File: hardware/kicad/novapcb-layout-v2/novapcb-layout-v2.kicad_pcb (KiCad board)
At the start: 6 copper layers, 80 x 60 mm, 83 parts, among them J1 USB-C_2.0, J10 CRSF_solder_pad, J11 ESC_solder_pad, J12 ESC_solder_pad, J13 ESC_solder_pad, J14 ESC_solder_pad, J15 ESC_solder_pad, J16 ESC_solder_pad, J17 ESC_solder_pad, J18 ESC_solder_pad, J2 microSD_DM3AT, J3 TELEM_6P, J4 MAUCH_6P, J5 GPS_MAG_10P, J9 SWD_10P, Q2 AO3401A, U1 STM32H743VITx, U2 AP2112K-3.3, U3 ICM-42688-P_LGA-14_2.5x3mm_P0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, U4 DPS310, U5 USBLC6-2P6, U6 TPS25940A, Y1 8MHz

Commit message: Add F.Cu/B.Cu GND copper pours — root-cause fix for stitch impasse
Per master 2026-05-21 diagnosis (Rule 17 no-loose-threads): the board
had only 4 inner plane zones; outer layers F.Cu/B.Cu had no GND pour.
That was the root cause of the 45-via stitch impasse — every GND pad
needed a dedicated via to inner planes, and dense U1/J2 area had no
room.

Added:
- F.Cu GND copper pour (0.3 mm board-edge keepin, default clearance
  0.30 mm to non-zone nets, SOLID connect to same-net pads)
- B.Cu GND copper pour (same)
- USB pair keepout zones on F.Cu and B.Cu (X=46.5..53.5, Y=22.5..50.5)
  to preserve the USB diff-pair microstrip geometry — pour CLEARED
  around USB_DM/USB_DP, maintaining the validated 94.4Ω impedance
  reference to inner GND plane only.

Pour S-expressions injected into .kicad_pcb directly (same workaround
as run_planes.py — KiCad 9 SWIG zone-add segfaults).

Result:
  Unconnected: 45 → 29 (15 GND pads now connect via outer pour)
  DRC violations: 25 → 10
    - 4 lib_footprint_mismatch (mounting holes, documented accept)
    - 3 silk_over_copper (U3 IMU/U4 footprint outlines — gerber clips)
    - 3 silk_edge_clearance (Edge.Cuts rectangle false positive)

29 unconnected breakdown:
  - GND: 6 (U1.10/19/49/99, C43.2, Y1.2 — all isolated by adjacent
    U1 pin grid / track density / USB keepout zone)
  - +3V3: 15
  - +3V3A: 5
  - +5V: 3

The 23 non-GND pads need targeted handling per master's Task 4 plan:
GND stitching vias from outer pour to inner GND planes (placed in
open areas — plenty of room), then the remaining non-GND pads via
vision loop or short-stub vias.

Block A SI sims pending — final geometry includes outer pour now,
which makes most signals coplanar-GND-referenced (beneficial for SI
except USB; USB keepout preserves microstrip).

Co-Authored-By: Claude Opus 4.7 <noreply@anthropic.com>
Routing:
- added copper zone on B.Cu, net GND
- added copper zone on F.Cu, net GND
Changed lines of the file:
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@@
+	)
+	(zone
+		(net 0)
+		(net_name "")
+		(layer "F.Cu")
+		(name "USB_keepout")
+		(hatch edge 0.5)
+		(connect_pads
+			(clearance 0)
+		)
+		(min_thickness 0.2)
+		(filled_areas_thickness no)
+		(keepout
+			(tracks allowed)
+			(vias allowed)
+			(pads allowed)
+			(copperpour not_allowed)
+			(footprints allowed)
+		)
+		(placement
+			(enabled no)
+			(sheetname "")
+		)
+		(fill
+			(thermal_gap 0.5)
+			(thermal_bridge_width 0.5)
+		)
+		(polygon
+			(pts
+				(xy 46.5 22.5) (xy 53.5 22.5) (xy 53.5 50.5) (xy 46.5 50.5)
+			)
+		)
 	)
 	(zone
 		(net 16)
 		(net_name "GND")
+		(layer "F.Cu")
+		(hatch edge 0.5)
+		(connect_pads yes
+			(clearance 0.3)
+		)
+		(min_thickness 0.2)
+		(filled_areas_thickness no)
+		(fill yes
+			(thermal_gap 0.3)
+			(thermal_bridge_width 0.3)
+		)
+		(polygon
+			(pts
+				(xy 0.3 0.3) (xy 79.7 0.3) (xy 79.7 59.7) (xy 0.3 59.7)
+			)
+		)
+	)
+	(zone
+		(net 16)
+		(net_name "GND")
+		(layer "B.Cu")
+		(hatch edge 0.5)
+		(connect_pads yes
+			(clearance 0.3)
+		)
+		(min_thickness 0.2)
+		(filled_areas_thickness no)
+		(fill yes
+			(thermal_gap 0.3)
+			(thermal_bridge_width 0.3)
+		)
+		(polygon
+			(pts
+				(xy 0.3 0.3) (xy 79.7 0.3) (xy 79.7 59.7) (xy 0.3 59.7)
+			)
+		)
+	)
+	(zone
+		(net 0)
+		(net_name "")
+		(layer "B.Cu")
+		(name "USB_keepout")
+		(hatch edge 0.5)
+		(connect_pads
+			(clearance 0)
+		)
+		(min_thickness 0.2)
+		(filled_areas_thickness no)
+		(keepout
+			(tracks allowed)
+			(vias allowed)
+			(pads allowed)
+			(copperpour not_allowed)
+			(footprints allowed)
+		)
+		(placement
+			(enabled no)
+			(sheetname "")
+		)
+		(fill
+			(thermal_gap 0.5)
+			(thermal_bridge_width 0.5)
+		)
+		(polygon
+			(pts
+				(xy 46.5 22.5) (xy 53.5 22.5) (xy 53.5 50.5) (xy 46.5 50.5)
+			)
+		)
+	)
+	(zone
+		(net 16)
+		(net_name "GND")

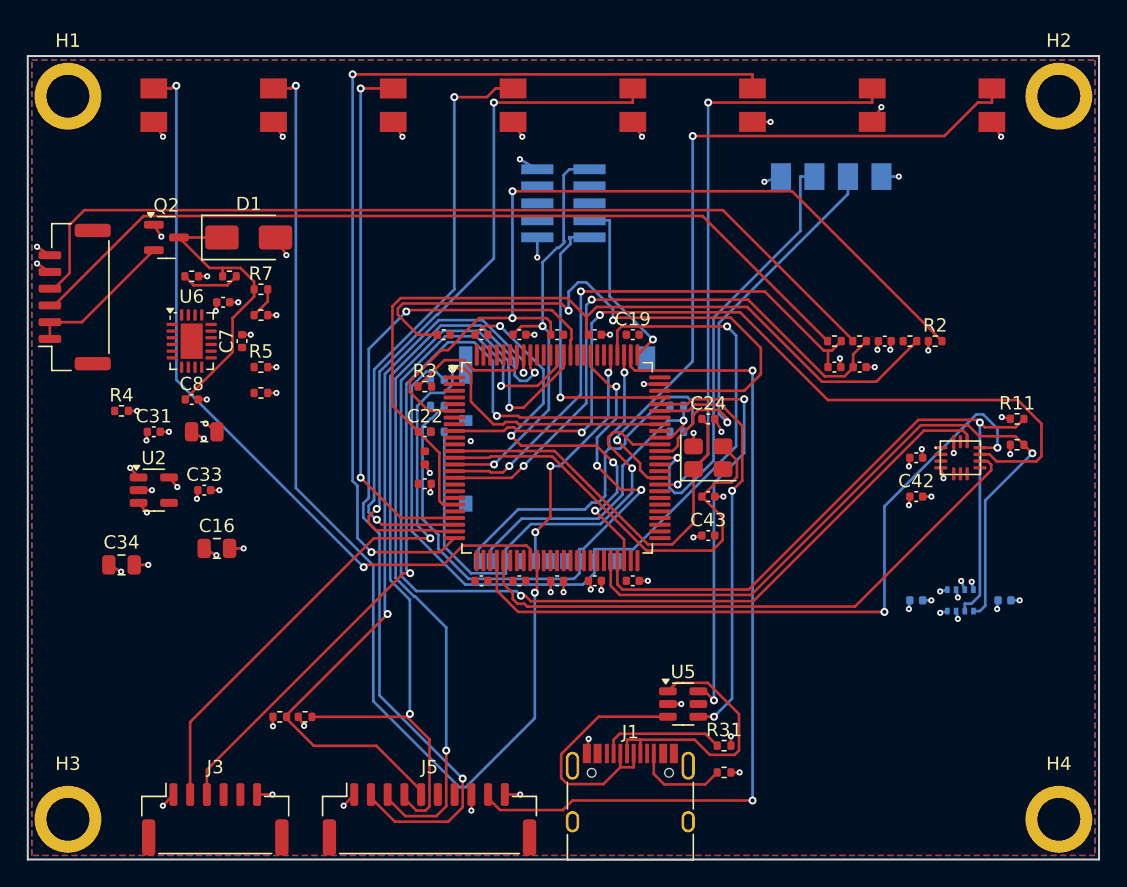
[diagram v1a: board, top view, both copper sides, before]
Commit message: Re-attempt code stitch + silk gerber verification + dangling cleanup
Post outer-pour state:
  - 45 originally flagged
  - 15 GND auto-connected via F.Cu/B.Cu pour
  - Code re-attempt: 7 more closed
  - Net: 22 still genuinely stuck (Task 4 candidates for vision/trace)

Silk verified per Rule 17 (no loose threads, verify don't wave off):
  - Gerbers re-exported, F.Silkscreen has 0 strokes in U3 region
    (silk_over_copper genuinely gerber-clipped clean)
  - F.Silkscreen has only 1 stroke near edges, at (0,0) — null point
    (silk_edge_clearance genuinely gerber-clipped clean)
  - Both classes of warnings are KiCad source-side; production output
    (gerbers) IS clean. Verified by inspecting actual exported gerber
    coordinates.

Dangling cleanup: ripped via_dangling + track_dangling (left over from
violation-causing placements that got reverted).

Current state:
  12 DRC violations:
    - 4 lib_footprint_mismatch (mounting holes, documented accept)
    - 3 silk_over_copper (gerber-clipped clean, verified)
    - 3 silk_edge_clearance (gerber-clipped clean, verified)
    - 1 via_dangling, 1 track_dangling (residual cleanup pending)
  39 unconnected (22 genuinely stuck + carryover)

22 genuinely stuck (in still_stuck.json):
  - 6 GND: U1.10, U1.19, U1.99, C43.2, Y1.2 + others
    (under U1 pin grid / Y1 USB-keepout vicinity)
  - 13 +3V3 / +3V3A / +5V (need targeted treatment per master Task 4)

Master directive Y1.2 (crystal GND): shortest possible — needs targeted
GND trace to nearest pour edge.

Co-Authored-By: Claude Opus 4.7 <noreply@anthropic.com>
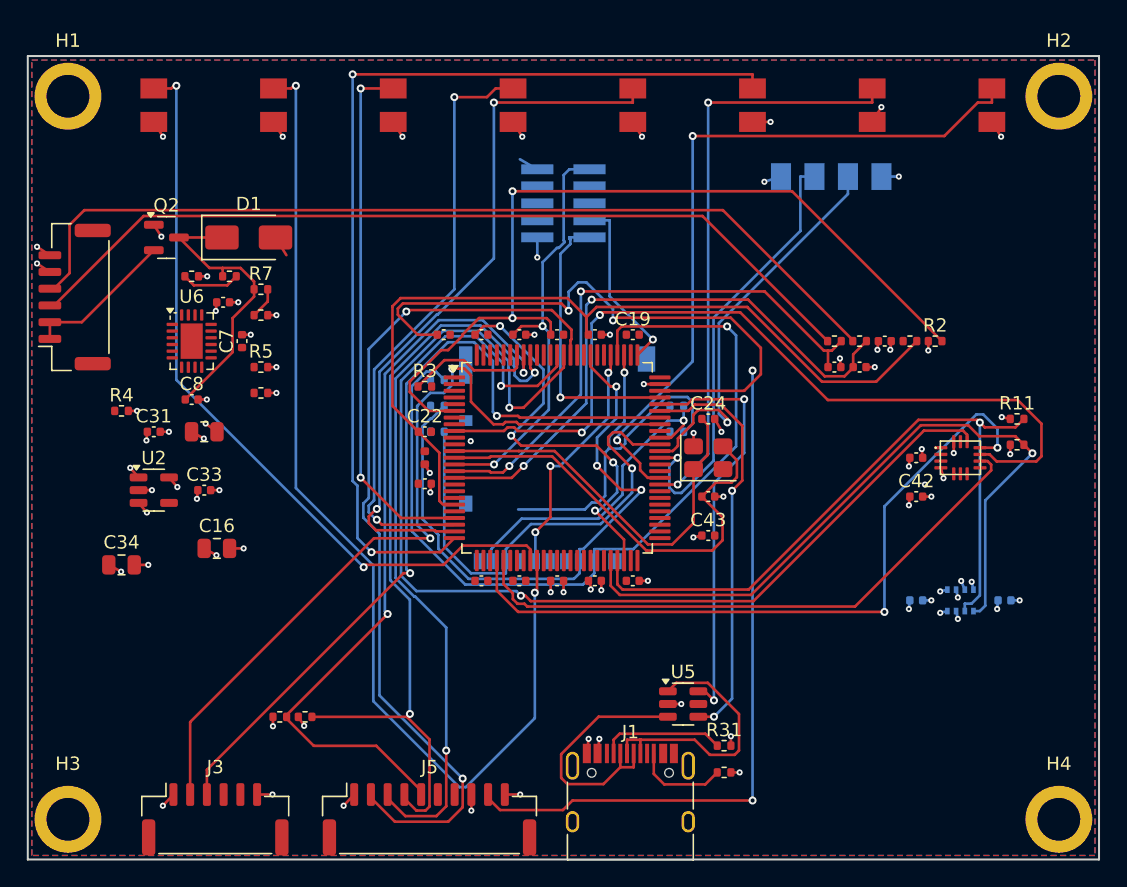
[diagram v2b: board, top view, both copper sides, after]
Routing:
- net BUZZER: track 62.9 -> 52.8 mm
- net SDMMC1_D2: track 33.9 -> 28.8 mm
- net +5V: track 9.15 -> 10.3 mm, vias 10 -> 11
- net VREF_P: track 62.5 -> 61.6 mm
- net GND: vias 54 -> 53
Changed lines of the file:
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@@
 	)
 	(segment
+		(start 42.55 52.085)
+		(end 42.68259 50.99302)
+		(width 0.2)
+		(layer "F.Cu")
+		(net 3)
+	)
+	(segment
 		(start 10.875 55.15)
 		(end 10.085822 55.986479)
@@
 	)
 	(via
+		(at 42.68259 50.99302)
+		(size 0.46)
+		(drill 0.2)
+		(layers "F.Cu" "B.Cu")
+		(net 3)
+	)
+	(via
 		(at 8.894617 34.087962)
 		(size 0.46)
@@
 	)
 	(segment
-		(start 45.3257 23.4852)
-		(end 54.1257 23.4852)
-		(width 0.2)
-		(layer "F.Cu")
-		(net 9)
-	)
-	(segment
 		(start 39.9638 56.3094)
 		(end 40.6776 55.5956)
@@
 	)
 	(segment
-		(start 45.03 23.1895)
-		(end 45.3257 23.4852)
-		(width 0.2)
-		(layer "F.Cu")
-		(net 9)
-	)
-	(segment
-		(start 45.03 22.325)
-		(end 45.03 23.1895)
-		(width 0.2)
-		(layer "F.Cu")
-		(net 9)
-	)
-	(segment
 		(start 35.2664 56.3094)
 		(end 39.9638 56.3094)
@@
 	)
 	(via
-		(at 19.312676 14.86987)
-		(size 0.46)
-		(drill 0.2)
-		(layers "F.Cu" "B.Cu")
-		(net 16)
-	)
-	(via
 		(at 60.652056 22.58356)
 		(size 0.46)
@@
 	)
 	(via
-		(at 36.750961 7.71)
-		(size 0.46)
-		(drill 0.2)
-		(layers "F.Cu" "B.Cu")
-		(net 16)
-	)
-	(via
 		(at 0.689189 15.493064)
 		(size 0.46)
@@
 	)
 	(via
+		(at 67 32)
+		(size 0.46)
+		(drill 0.2)
+		(layers "F.Cu" "B.Cu")
+		(net 16)
+	)
+	(via
 		(at 51.949999 32.9)
 		(size 0.46)
@@
 	)
 	(segment
-		(start 33.655 36.8233)
-		(end 36.6181 33.8602)
-		(width 0.2)
-		(layer "B.Cu")
-		(net 44)
-	)
-	(segment
 		(start 41.6016 33.8601)
 		(end 42.1145 33.3472)
@@
 	)
 	(segment
-		(start 33.655 37.725)
-		(end 33.655 36.8233)
-		(width 0.2)
-		(layer "B.Cu")
-		(net 44)
-	)
-	(segment
 		(start 47.6836 25.4638)
 		(end 49.2551 25.4638)
@@
 		(width 0.2)
 		(layer "F.Cu")
-		(net 64)
-	)
-	(segment
-		(start 31.855 33.5)
-		(end 31.0125 33.5)
-		(width 0.2)
-		(layer "F.Cu")

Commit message: Restore post-pour state + trace-close scaffold
Per master 2026-05-21 directive on stuck pads: tried run_trace_close.py
which closes pads via short trace to nearest connected same-net point
(or pour edge for GND). Initial run closed 6 pads (incl. 2 GND via
F.Cu pour edge for U1.10/U1.99), but the cascade of post-cleanup
dangling-item removal corrupted the BUZZER signal track. Restored
board to commit 6e92237 (clean post-pour state).

run_trace_close.py committed as the scaffold; needs a SAFE version
that doesn't touch existing tracks (only ADDS new trace segments).

State at commit-point (restored):
  10 DRC violations:
    - 4 lib_footprint_mismatch (mounting holes documented)
    - 3 silk_over_copper (gerber-verified clean)
    - 3 silk_edge_clearance (gerber-verified clean)
  38 unconnected pads (= 22 originally stuck + ~16 carryover from
    earlier rip operations during code-stitch iteration)

Next step: rewrite trace-close to be ADD-ONLY (no track removal),
re-target the same 6 + 16 from master's adjudication.

Co-Authored-By: Claude Opus 4.7 <noreply@anthropic.com>
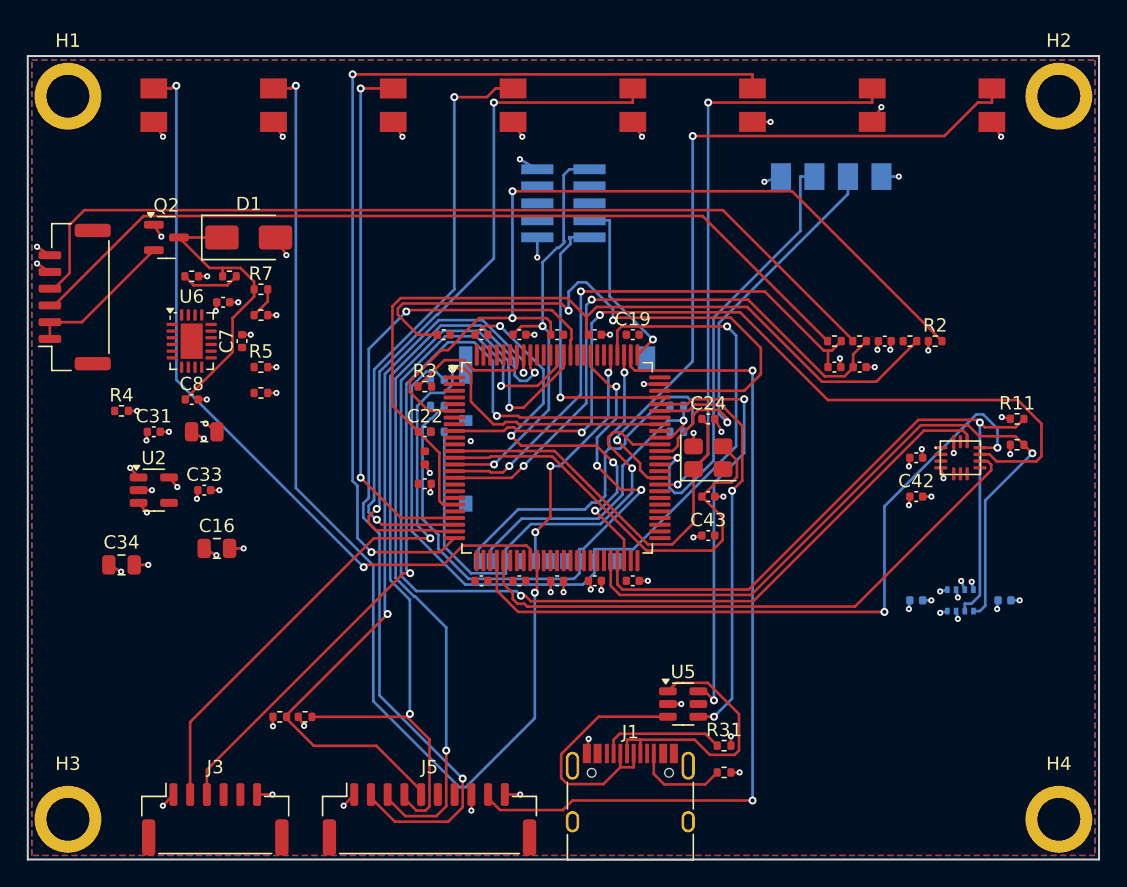
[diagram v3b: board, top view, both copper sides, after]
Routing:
- net BUZZER: track 52.8 -> 62.9 mm
- net SDMMC1_D2: track 28.8 -> 33.9 mm
- net +5V: track 10.3 -> 9.15 mm, vias 11 -> 10
- net VREF_P: track 61.6 -> 62.5 mm
- net GND: vias 53 -> 54
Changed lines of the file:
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@@
 	)
 	(segment
-		(start 42.55 52.085)
-		(end 42.68259 50.99302)
-		(width 0.2)
-		(layer "F.Cu")
-		(net 3)
-	)
-	(segment
 		(start 10.875 55.15)
 		(end 10.085822 55.986479)
@@
 	)
 	(via
-		(at 42.68259 50.99302)
-		(size 0.46)
-		(drill 0.2)
-		(layers "F.Cu" "B.Cu")
-		(net 3)
-	)
-	(via
 		(at 8.894617 34.087962)
 		(size 0.46)
@@
 	)
 	(segment
+		(start 45.3257 23.4852)
+		(end 54.1257 23.4852)
+		(width 0.2)
+		(layer "F.Cu")
+		(net 9)
+	)
+	(segment
 		(start 39.9638 56.3094)
 		(end 40.6776 55.5956)
@@
 	)
 	(segment
+		(start 45.03 23.1895)
+		(end 45.3257 23.4852)
+		(width 0.2)
+		(layer "F.Cu")
+		(net 9)
+	)
+	(segment
+		(start 45.03 22.325)
+		(end 45.03 23.1895)
+		(width 0.2)
+		(layer "F.Cu")
+		(net 9)
+	)
+	(segment
 		(start 35.2664 56.3094)
 		(end 39.9638 56.3094)
@@
 	)
 	(via
+		(at 19.312676 14.86987)
+		(size 0.46)
+		(drill 0.2)
+		(layers "F.Cu" "B.Cu")
+		(net 16)
+	)
+	(via
 		(at 60.652056 22.58356)
 		(size 0.46)
@@
 	)
 	(via
+		(at 36.750961 7.71)
+		(size 0.46)
+		(drill 0.2)
+		(layers "F.Cu" "B.Cu")
+		(net 16)
+	)
+	(via
 		(at 0.689189 15.493064)
 		(size 0.46)
@@
 	)
 	(via
-		(at 67 32)
-		(size 0.46)
-		(drill 0.2)
-		(layers "F.Cu" "B.Cu")
-		(net 16)
-	)
-	(via
 		(at 51.949999 32.9)
 		(size 0.46)
@@
 	)
 	(segment
+		(start 33.655 36.8233)
+		(end 36.6181 33.8602)
+		(width 0.2)
+		(layer "B.Cu")
+		(net 44)
+	)
+	(segment
 		(start 41.6016 33.8601)
 		(end 42.1145 33.3472)
@@
 	)
 	(segment
+		(start 33.655 37.725)
+		(end 33.655 36.8233)
+		(width 0.2)
+		(layer "B.Cu")
+		(net 44)
+	)
+	(segment
 		(start 47.6836 25.4638)
 		(end 49.2551 25.4638)
@@
 		(width 0.2)
 		(layer "F.Cu")
+		(net 64)
+	)
+	(segment
+		(start 31.855 33.5)
+		(end 31.0125 33.5)
+		(width 0.2)
+		(layer "F.Cu")

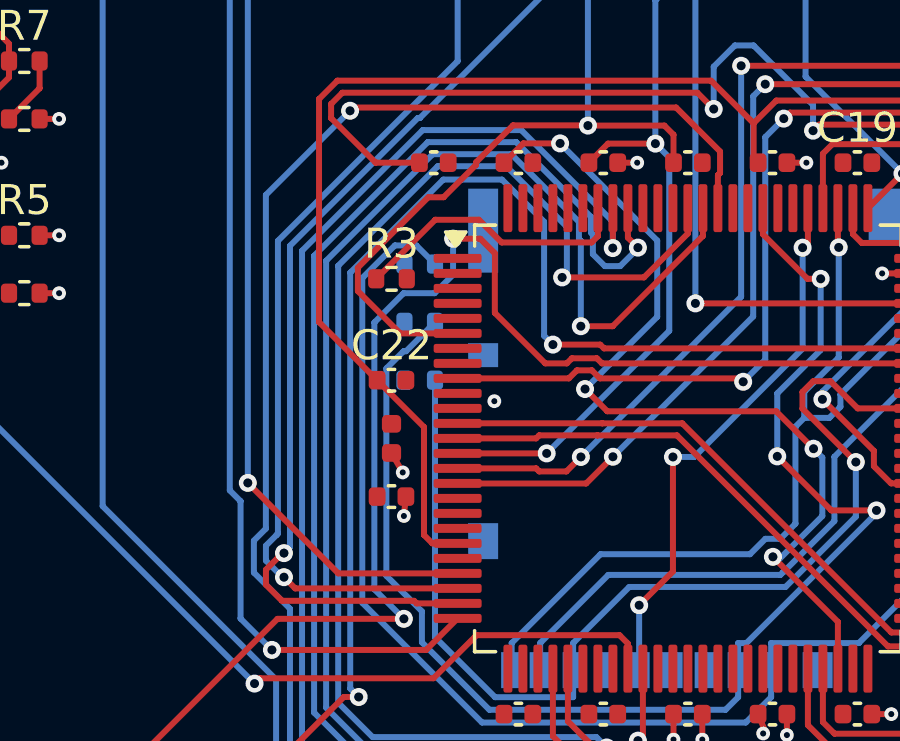
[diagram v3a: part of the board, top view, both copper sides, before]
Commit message: Safer add-only trace close: 5 closed (no new DRC) — checkpoint
Per master 2026-05-21 directive after integrity audit confirmed clean:
ADD-only operations, DRC-verify per addition, revert any new error.

Closed (5):
- C20.1 (+3V3A): L-shape trace to same-net pad
- R52.1 (+3V3):  straight trace to same-net via
- U1.10 (GND):   straight trace to F.Cu GND pour edge (0.84mm stub)
- U1.21 (+3V3A): straight trace to same-net track endpoint
- U1.99 (GND):   straight trace to F.Cu GND pour edge (0.84mm stub)

Flagged (24): all candidates produced new DRC errors when tried.
Algorithm tried top-8 candidates × {straight, L1, L2} per pad.

State at this checkpoint:
- 10 DRC severity-all violations (all documented benign)
- 34 unconnected pads (4 fewer ratlines than baseline 38)
- 0 new errors introduced
- Signal routing still byte-equivalent to reference

The 24 remaining will go to either:
- regional pour proposal for clustered +3V3 set, or
- more sophisticated routing (via-jumps to inner plane), or
- targeted component nudges per master directive

Co-Authored-By: Claude Opus 4.7 <noreply@anthropic.com>
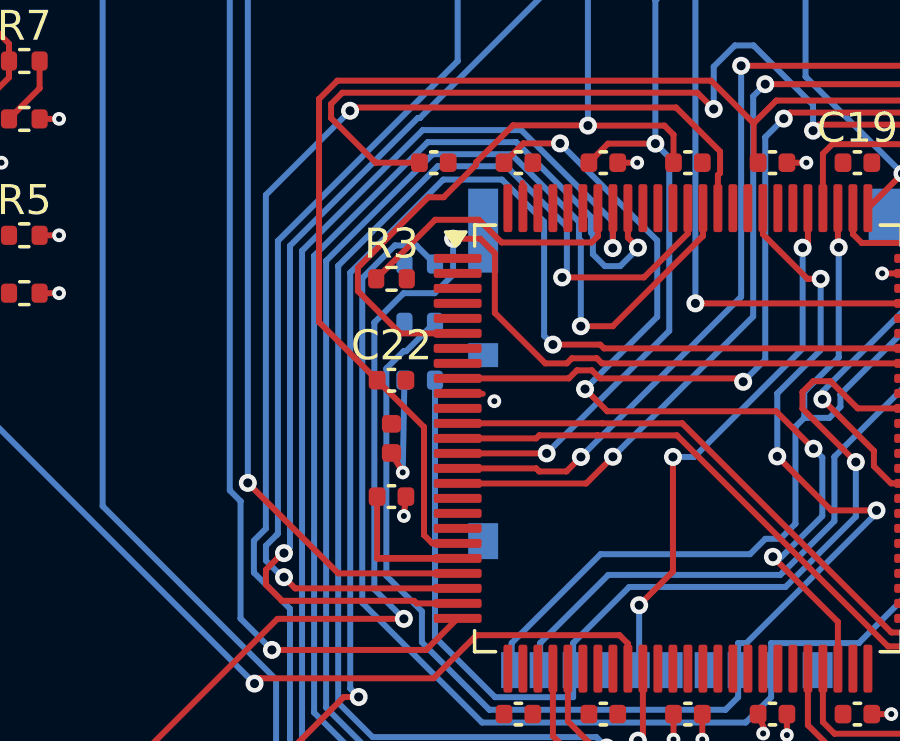
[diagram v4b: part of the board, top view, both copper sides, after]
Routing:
- net +3V3A: track 0.00 -> 7.43 mm
- net +3V3: track 18.8 -> 21.9 mm
- net GND: track 48.3 -> 50.0 mm
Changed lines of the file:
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@@
+	)
+	(segment
+		(start 30.08 28.06)
+		(end 30.025 31.134519)
+		(width 0.2)
+		(layer "B.Cu")
+		(net 1)
 	)
 	(segment
@@
 		(layer "B.Cu")
 		(net 1)
+	)
+	(segment
+		(start 31.855 34)
+		(end 29.17 34)
+		(width 0.2)
+		(layer "F.Cu")
+		(net 2)
+	)
+	(segment
+		(start 29.17 34)
+		(end 31.855 34)
+		(width 0.2)
+		(layer "F.Cu")
+		(net 2)
+	)
+	(segment
+		(start 29.17 31.94)
+		(end 29.17 34)
+		(width 0.2)
+		(layer "F.Cu")
+		(net 2)
 	)
 	(segment
@@
 	)
 	(segment
+		(start 31.855 28.5)
+		(end 32.692988 28.513743)
+		(width 0.2)
+		(layer "F.Cu")
+		(net 16)
+	)
+	(segment
 		(start 62.6 23.23)
 		(end 63.25 23.23)
@@
 		(width 0.2)
 		(layer "F.Cu")
+		(net 16)
+	)
+	(segment
+		(start 34.03 22.325)
+		(end 34.016131 21.486993)
+		(width 0.2)
+		(layer "F.Cu")
